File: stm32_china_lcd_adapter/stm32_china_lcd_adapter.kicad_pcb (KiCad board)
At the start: 2 copper layers, 38 x 28 mm, 19 parts, among them J1 - To LCD China_40P_LCD, J2 - To MCU China_40P_LCD, J3 China_6P_CTP, U1 MT9284-28J

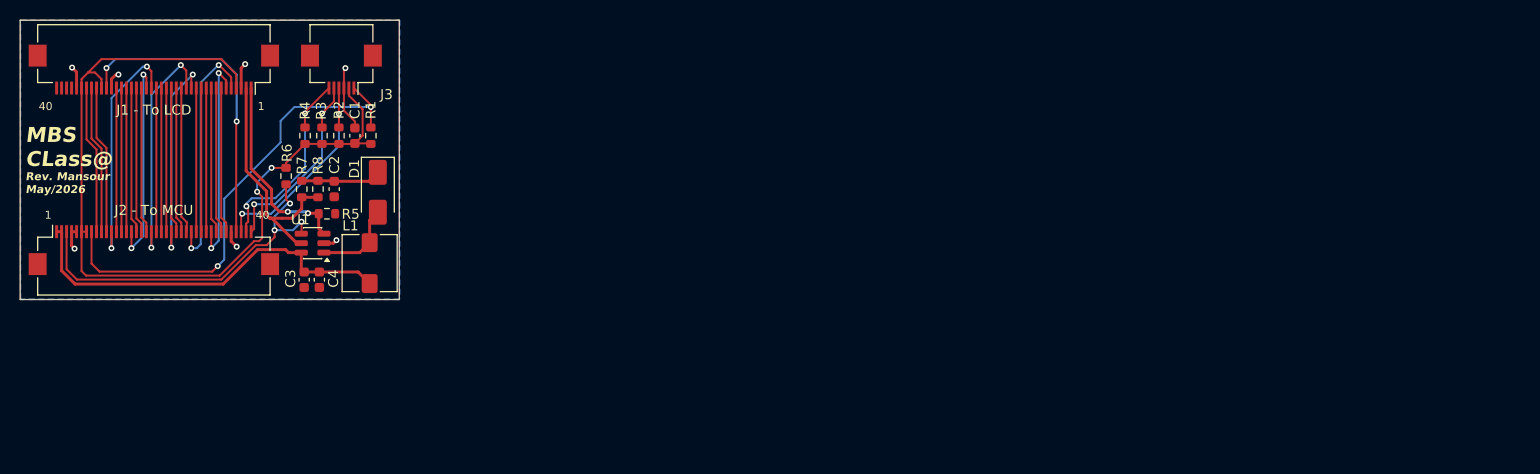
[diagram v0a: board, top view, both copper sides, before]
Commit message: upgradinng lcd adapter with blacklight power
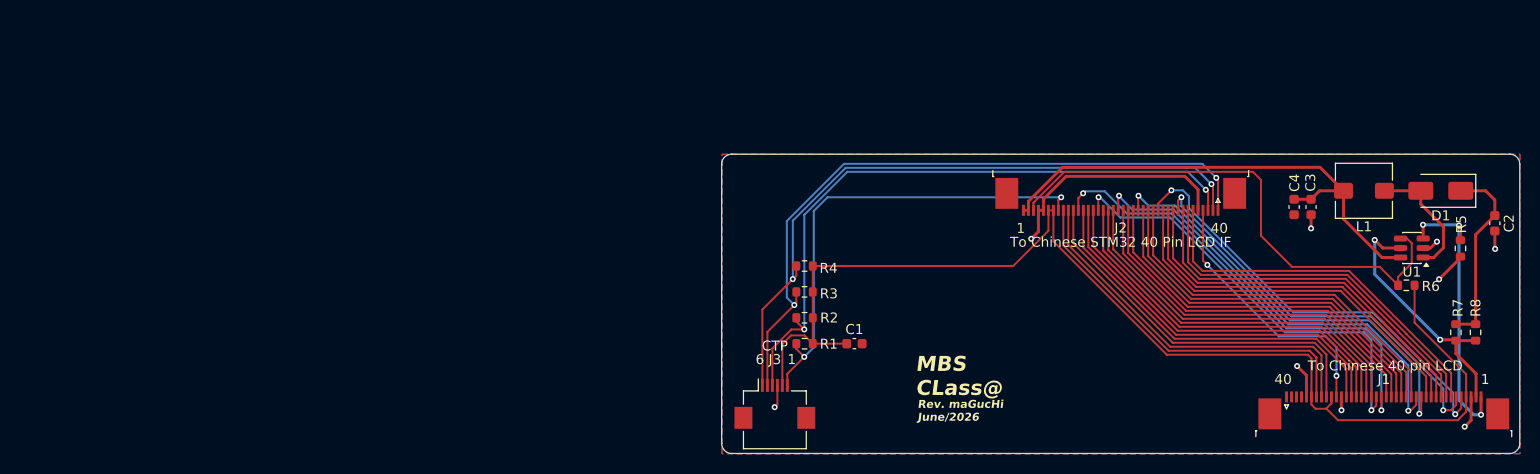
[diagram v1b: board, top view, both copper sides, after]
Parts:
- removed J1 - To LCD: China_40P_LCD, Connector_FFC-FPC:Hirose_FH12-40S-0.5SH_1x40-1MP_P0.50mm_Horizontal
- removed J2 - To MCU: China_40P_LCD, Connector_FFC-FPC:Hirose_FH12-40S-0.5SH_1x40-1MP_P0.50mm_Horizontal
- removed REF**: OSHW-Symbol_6.7x6mm_SilkScreen, Symbol:OSHW-Symbol_6.7x6mm_SilkScreen
- added J1: China_40P_LCD, Connector_FFC-FPC:TE_4-1734839-0_1x40-1MP_P0.5mm_Horizontal, F.Cu at (211.0, 87.7)
- added J2: STM32_40P_LCD, Connector_FFC-FPC:TE_4-1734839-0_1x40-1MP_P0.5mm_Horizontal, F.Cu at (184.7, 66.3)
- moved R8 116.9 mm to (220.2, 79.8)
- moved R7 116.6 mm to (218.3, 79.8)
- moved C2 116.4 mm to (222.2, 68.9)
- moved R5 113.7 mm to (218.7, 71.4), turned to -90 degrees
- moved R6 112.8 mm to (213.3, 75.1), turned to 0 degrees
- moved U1 110.2 mm to (213.8, 71.4)
- moved D1 106.6 mm to (216.8, 65.7), turned to 180 degrees
- moved C3 101.2 mm to (203.8, 67.3)
- moved L1 99.9 mm to (209.1, 65.7), turned to 180 degrees
- moved C4 98.0 mm to (202.1, 67.3)
- moved J3 54.9 mm to (150.0, 87.0), turned to 0 degrees
- moved C1 54.2 mm to (158.0, 81.0), turned to 0 degrees
- moved R4 51.8 mm to (153.0, 73.2), turned to 180 degrees
- moved R3 50.8 mm to (153.0, 75.8), turned to 180 degrees
- moved R2 50.1 mm to (153.0, 78.4), turned to 180 degrees
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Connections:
- J3 pad 1: /CTP_RST -> /CTP_SCL
- J3 pad 2: /3V3 -> /CTP_SDA
- J3 pad 3: GND -> /CTP_INT
- J3 pad 4: /CTP_INT -> GND
- J3 pad 5: /CTP_SDA -> /3V3
- J3 pad 6: /CTP_SCL -> /CTP_RST
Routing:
- net /CTP_SDA: track 20.5 -> 68.6 mm
- net /CTP_SCL: track 20.8 -> 66.8 mm
- net /CTP_INT: track 21.5 -> 65.6 mm
- net /3V3: track 86.0 -> 118.3 mm, vias 2 -> 0
- net /LCD_R5: track 14.1 -> 38.2 mm
- net /LCD_R6: track 14.3 -> 38.3 mm
- net /LCD_R7: track 14.4 -> 38.2 mm
- net /LCD_G6: track 14.2 -> 38.0 mm
- net /LCD_G5: track 14.2 -> 38.0 mm
- net GND: track 18.5 -> 42.2 mm, vias 7 -> 9
- net /LCD_B7: track 14.4 -> 38.0 mm
- net /LCD_B5: track 14.4 -> 38.0 mm
- net /LCD_B6: track 14.4 -> 38.0 mm
- net /LCD_G7: track 14.4 -> 37.9 mm
- net /LCD_R3: track 14.6 -> 38.0 mm
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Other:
- board size 38 x 28 mm -> 80 x 30 mm
- board text added: "6"
- board text added: "CTP"
- board text added: "Rev. maGucHi June/2026"
- board text added: "To Chinese 40 pin LCD"
- board text added: "To Chinese STM32 40 Pin LCD IF"
- board text removed: "Rev. Mansour May/2026"
